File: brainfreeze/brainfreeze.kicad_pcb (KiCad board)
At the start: 4 copper layers, 69.6 x 106.9 mm, 13 parts, among them J1 XT30PW-M, P1 OSTTE020104, Q1 DMN63D8L-7, U1 H3LIS331DL, U3 AP63205WU

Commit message: updated with screwholes
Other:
- outline, holes or cut-outs redrawn
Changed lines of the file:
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@@
 		(tags "Arduino Nano")
 		(property "Reference" "A1"
-			(at 7.62 -5.08 0)
+			(at -0.37 -5.58 0)
 			(layer "F.SilkS")
 			(effects
@@
 		(layer "Edge.Cuts")
 	)
+	(gr_circle
+		(center 84.41 153.2)
+		(end 85.61 154.1)
+		(stroke
+			(width 0.0381)
+			(type default)
+		)
+		(fill none)
+		(layer "Edge.Cuts")
+	)
+	(gr_circle
+		(center 105.73 113.2)
+		(end 107.23 113.2)
+		(stroke
+			(width 0.0381)
+			(type default)
+		)
+		(fill none)
+		(layer "Edge.Cuts")
+	)
+	(gr_circle
+		(center 129.41 153.2)
+		(end 130.61 154.1)
+		(stroke
+			(width 0.0381)
+			(type default)
+		)
+		(fill none)
+		(layer "Edge.Cuts")
+	)

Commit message: Created gerber files
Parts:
- added G***: LOGO, brainfreeze:frost.image, B.Cu at (200.6, 110.4)
- added J10: Conn_01x01_Pin, Connector_Wire:SolderWire-1sqmm_1x01_D1.4mm_OD2.7mm, F.Cu at (222.5, 103.5)
- added J11: Conn_01x01_Pin, Connector_Wire:SolderWire-1sqmm_1x01_D1.4mm_OD2.7mm, F.Cu at (177.5, 117.5)
- added J2: Conn_01x01_Pin, Connector_Wire:SolderWire-0.5sqmm_1x01_D0.9mm_OD2.1mm, F.Cu at (222.5, 132.5)
- added J3: Conn_01x01_Pin, Connector_Wire:SolderWire-1sqmm_1x01_D1.4mm_OD2.7mm, F.Cu at (222.5, 121.5)
- added J4: Conn_01x01_Pin, Connector_Wire:SolderWire-1sqmm_1x01_D1.4mm_OD2.7mm, F.Cu at (222.5, 127.0)
- added J5: Conn_01x01_Pin, Connector_Wire:SolderWire-1sqmm_1x01_D1.4mm_OD2.7mm, F.Cu at (222.5, 108.0)
- added J6: Conn_01x03_Socket, brainfreeze:ESC CON, F.Cu at (177.0, 81.5)
- added J7: Conn_01x03_Socket, brainfreeze:ESC CON, F.Cu at (177.1, 92.6)
- added J8: Conn_01x01_Pin, Connector_Wire:SolderWire-0.5sqmm_1x01_D0.9mm_OD2.1mm, F.Cu at (222.5, 98.5)
- A1: footprint Module:Arduino_Nano -> brainfreeze:NANO_FIT
- C1, C2, C3, C4, L1, U1, U3: moved to F.Cu
- J1: value XT30PW-M -> Conn_01x01_Pin; footprint brainfreeze:XT30PW-M -> Connector_Wire:SolderWire-1sqmm_1x01_D1.4mm_OD2.7mm
- moved A1 110.9 mm to (201.3, 142.0)
- moved R1 97.6 mm to (186.7, 150.0)
- moved D1 96.1 mm to (180.2, 150.0)
- moved U1 94.0 mm to (200.5, 80.0), turned to 0 degrees
- moved J1 91.3 mm to (177.5, 112.0)
- moved L1 88.9 mm to (204.9, 98.0)
- moved C3 88.5 mm to (197.5, 101.5), turned to 0 degrees
- moved C2 88.0 mm to (203.0, 105.0)
- moved U3 86.1 mm to (198.6, 98.0)
- moved C4 85.9 mm to (203.0, 101.5)
- moved C1 85.2 mm to (201.5, 97.5), turned to -90 degrees
- moved Q1 64.1 mm to (186.1, 124.5)
- moved P1 58.6 mm to (183.2, 135.0), turned to 180 degrees
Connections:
- A1 pad 11: unconnected-(A1-D8-Pad11) -> ESC_2
- A1 pad 12: unconnected-(A1-D9-Pad12) -> ESC_1
- A1 pad 14: unconnected-(A1-D11-Pad14) -> LED
- A1 pad 16: unconnected-(A1-D13-Pad16) -> NEOPIXEL LED
- A1 pad 2: unconnected-(A1-D0/RX-Pad2) -> RX
- A1 pad 21: unconnected-(A1-A2-Pad21) -> ESC_SIGNAL2
- A1 pad 22: unconnected-(A1-A3-Pad22) -> ESC_SIGNAL3
- A1 pad 5: unconnected-(A1-D2-Pad5) -> ESC_SIGNAL1
- A1 pad 9: LED -> unconnected-(A1-D6-Pad9)
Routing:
- net ESC_1: track 0.00 -> 64.9 mm
- net ESC_2: track 0.00 -> 51.2 mm, vias 0 -> 1
- net RX: track 0.00 -> 37.2 mm
- net SDA: track 40.9 -> 71.2 mm, vias 0 -> 3
- net SCL: track 40.4 -> 65.8 mm, vias 0 -> 3
- net NEOPIXEL LED: track 0.00 -> 23.6 mm
- net 3V3: track 52.9 -> 74.8 mm, vias 0 -> 2
- net INT1: track 34.2 -> 55.7 mm, vias 0 -> 1
- net +5V: track 17.9 -> 36.0 mm, vias 1 -> 4
- net +12V: track 10.9 -> 27.2 mm
- net GND: track 13.4 -> 3.53 mm, vias 4 -> 3
- net Net-(U3-BST): track 10.5 -> 4.16 mm, vias 2 -> 0
- net Net-(A1-D12): track 11.7 -> 5.52 mm
- net Net-(D1-A): track 3.74 -> 4.85 mm
- net Net-(U3-SW): track 2.29 -> 1.76 mm
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- added copper zone on F.Cu, net GND
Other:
- board size 69.6 x 106.9 mm -> 50 x 90 mm
- board text added: "3V3"
- board text added: "ACCELEROMETER"
- board text added: "BATTERY CONNECTOR"
- board text added: "BUCK CONVERTER CIRCUIT"
- board text added: "DESIGNED BY: Nathaniel Wheeler, Kamran Isfahani AND Pedro Coelho FOR UCONN FROST ROBOTICS"
- board text added: "ESC_1"
- board text added: "ESC_2"
- board text added: "GND"
- board text added: "HI-PWR LED SCREW CON"
- board text added: "INT1"
- board text added: "MOSFET"
- board text added: "PWR"
- board text added: "PWR INDICATOR LED"
- board text added: "RECIEVER"
- board text added: "SCL"
- board text added: "SDA"
- board text added: "SIG"
- board text added: "STATUS LED"

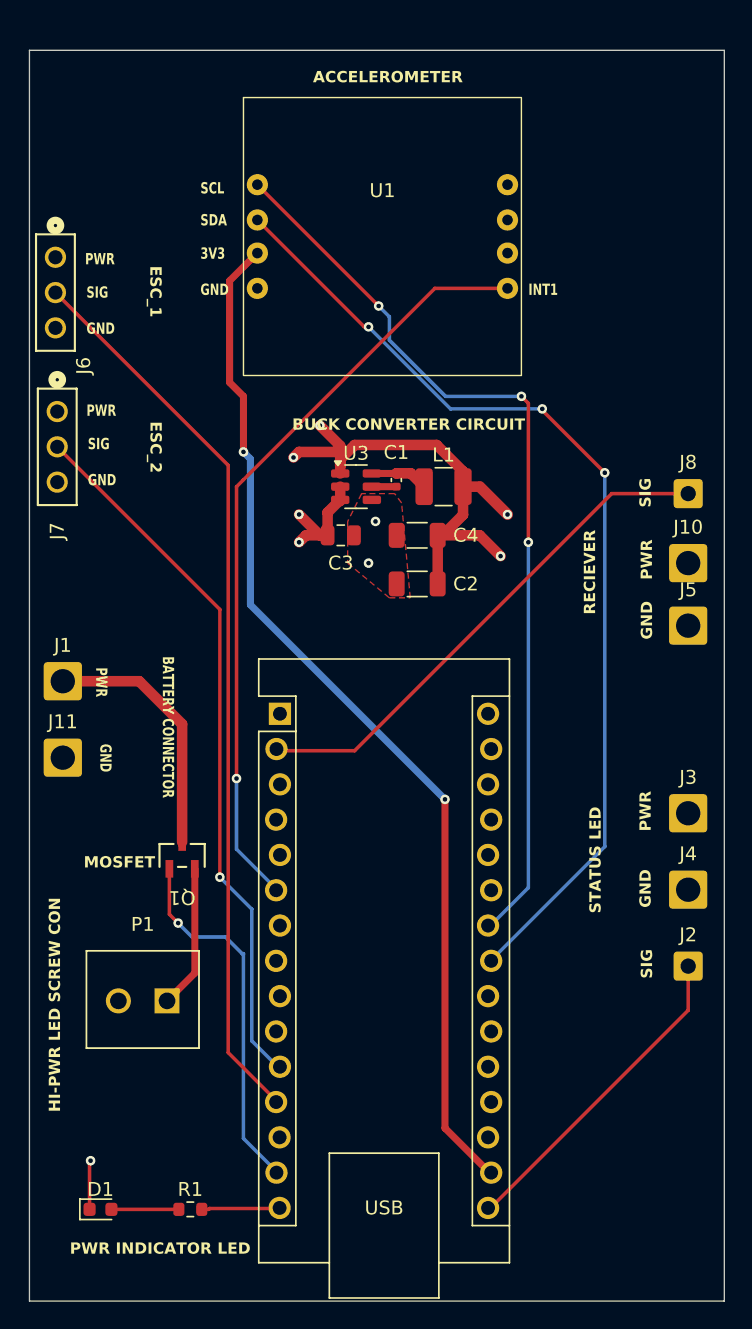
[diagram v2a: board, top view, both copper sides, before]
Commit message: added .gitignore for *.zip, fillet + dimensioned PCB
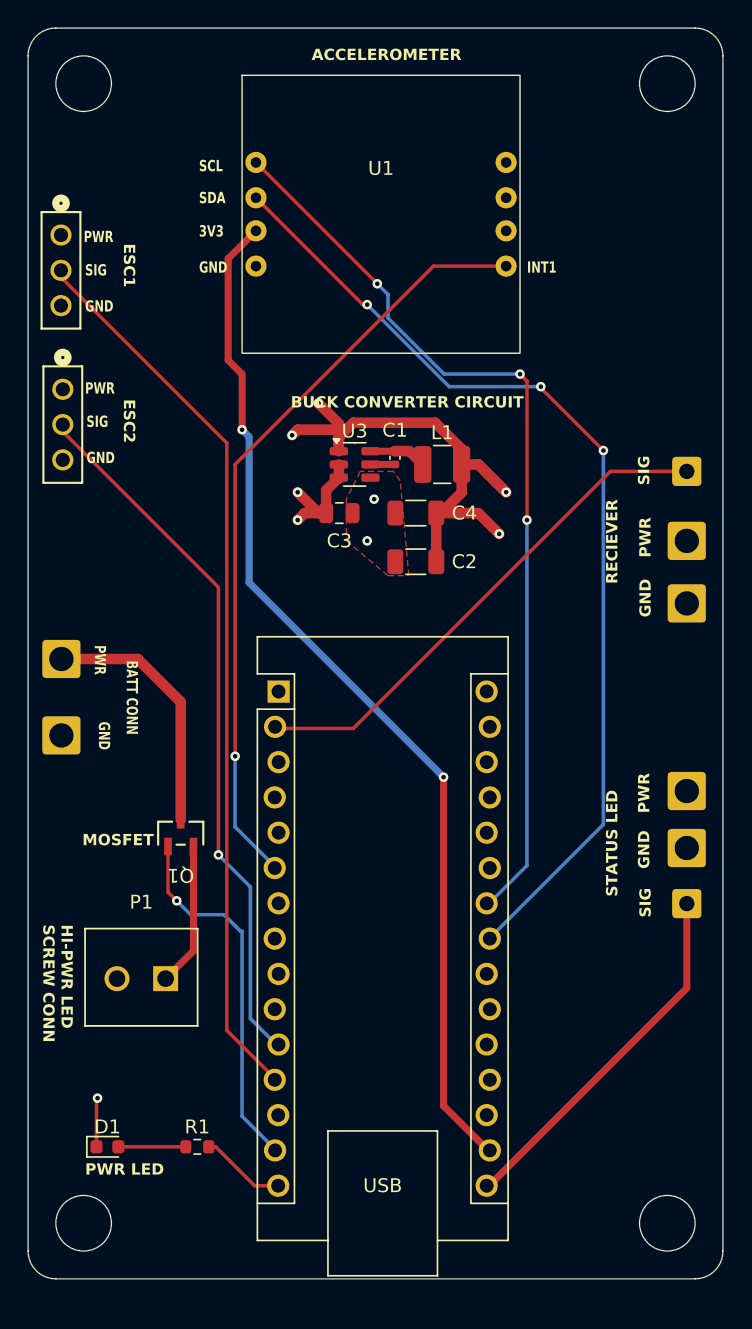
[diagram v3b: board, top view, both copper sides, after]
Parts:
- moved D1 4.53 mm to (180.7, 145.5)
- moved R1 4.53 mm to (187.2, 145.5)
- moved J2 4.50 mm to (222.4, 128.0)
- moved J4 3.00 mm to (222.4, 124.0)
- moved J7 1.65 mm to (177.5, 91.0)
- moved J6 1.65 mm to (177.4, 79.9)
- moved G*** 1.60 mm to (200.5, 108.8)
- moved Q1 1.60 mm to (186.0, 122.9)
- moved A1 1.60 mm to (201.2, 140.4)
- moved C1 1.60 mm to (201.4, 95.9)
- moved C2 1.60 mm to (202.9, 103.4)
- moved C3 1.60 mm to (197.4, 99.9)
- moved C4 1.60 mm to (202.9, 99.9)
- moved J1 1.60 mm to (177.4, 110.4)
- moved J10 1.60 mm to (222.4, 101.9)
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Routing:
- net NEOPIXEL LED: track 23.6 -> 26.5 mm
- net Net-(A1-D12): track 5.52 -> 6.16 mm
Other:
- outline, holes or cut-outs redrawn
- board text added: "BATT CONN"
- board text added: "ESC1"
- board text added: "ESC2"
- board text added: "HI-PWR LED SCREW CONN"
- board text added: "PWR LED"
- board text removed: "BATTERY CONNECTOR"
- board text removed: "ESC_1"
- board text removed: "ESC_2"
- board text removed: "HI-PWR LED SCREW CON"
- board text removed: "PWR INDICATOR LED"

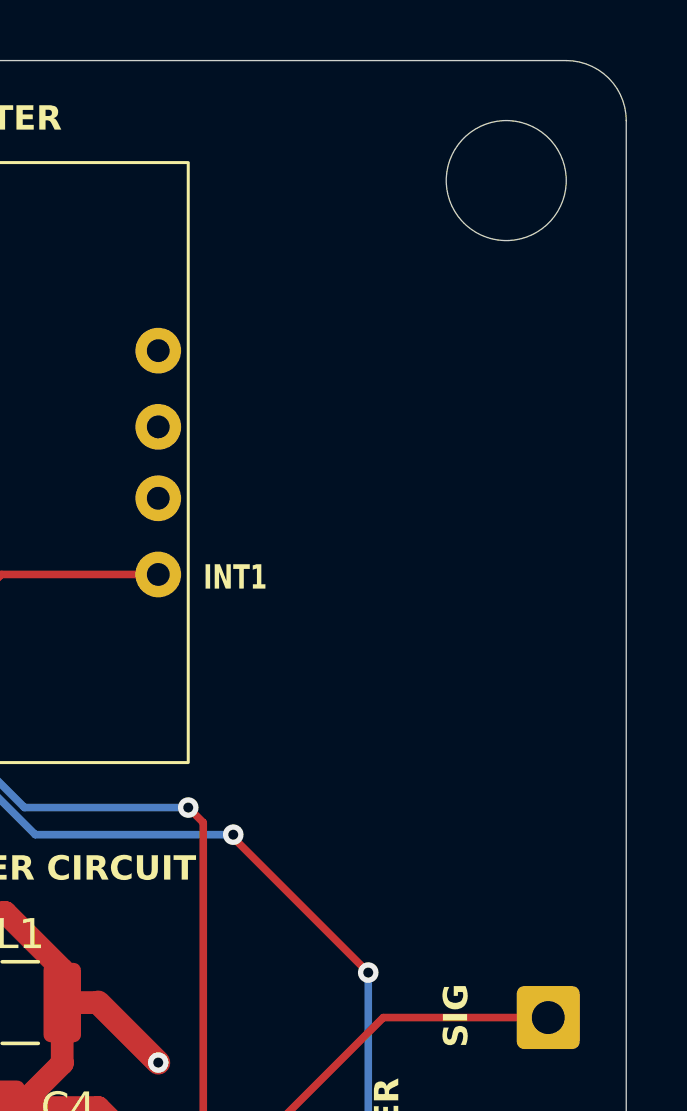
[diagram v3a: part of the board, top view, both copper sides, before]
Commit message: Added version number to board
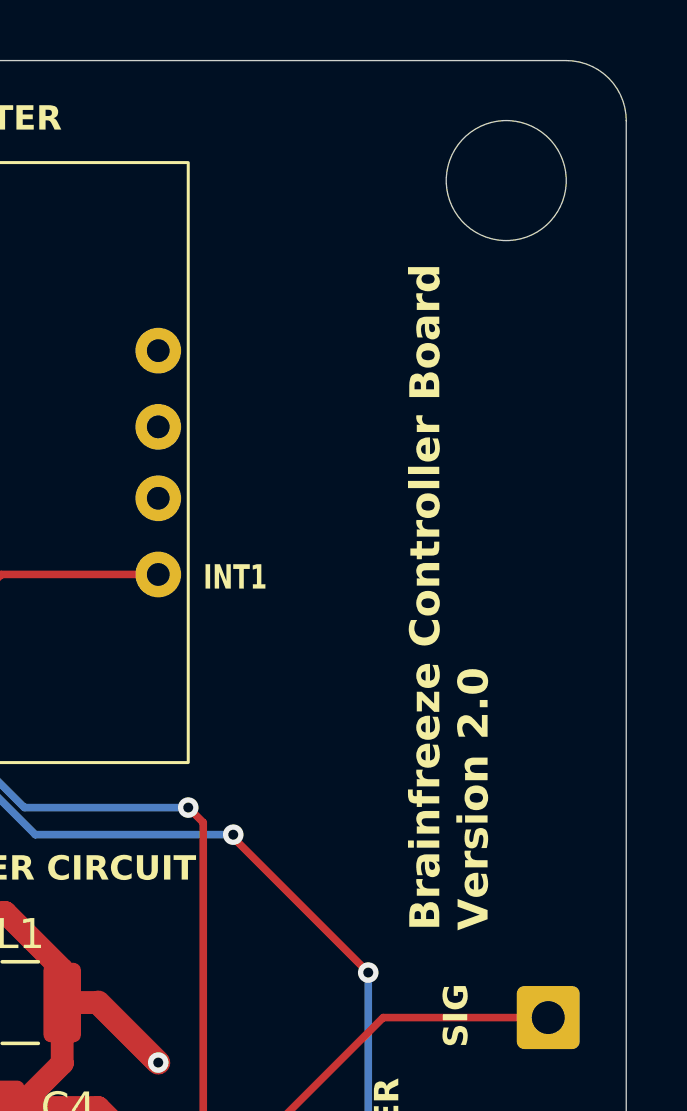
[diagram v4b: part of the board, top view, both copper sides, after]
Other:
- board text added: "Brainfreeze Controller Board Version 2.0"
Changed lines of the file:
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@@
+		)
+	)
+	(gr_text "Brainfreeze Controller Board\nVersion 2.0"
+		(at 220.5 94 90)
+		(layer "F.SilkS")
+		(effects
+			(font
+				(size 1 1)
+				(thickness 0.2)
+				(bold yes)
+			)
+			(justify left bottom)
 		)
 	)

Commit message: updated
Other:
- board text added: "DESIGNED BY: Nathaniel Wheeler, Kamran Isfahani, Pedro Coelho, AND Louis Spencer FOR UCONN FROST ROBOTICS"
- board text removed: "DESIGNED BY: Nathaniel Wheeler, Kamran Isfahani AND Pedro Coelho FOR UCONN FROST ROBOTICS"
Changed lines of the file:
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@@
 		)
 	)
-	(gr_text "DESIGNED BY: Nathaniel Wheeler, Kamran Isfahani AND Pedro Coelho \nFOR UCONN FROST ROBOTICS\n\n"
-		(at 216.5 154.5 0)
+	(gr_text "DESIGNED BY: Nathaniel Wheeler, Kamran Isfahani,\nPedro Coelho, AND Louis Spencer \nFOR UCONN FROST ROBOTICS\n\n"
+		(at 211.5 155.5 0)
 		(layer "B.SilkS")
 		(effects
